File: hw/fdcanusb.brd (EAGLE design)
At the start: 41 x 32 mm, 42 parts, among them J1 MF-CON-MICROUSB-RIGHT, J3 JST-ZH6SMT_VERT, M1 MOUNT, M2 MOUNT, M3 MOUNT, M4 MOUNT, U1 MF-REG-SOT235-3.3V-300mA, U2 USBLC6-2SC6, U3 TCAN1057AEV, U4 TLP3317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

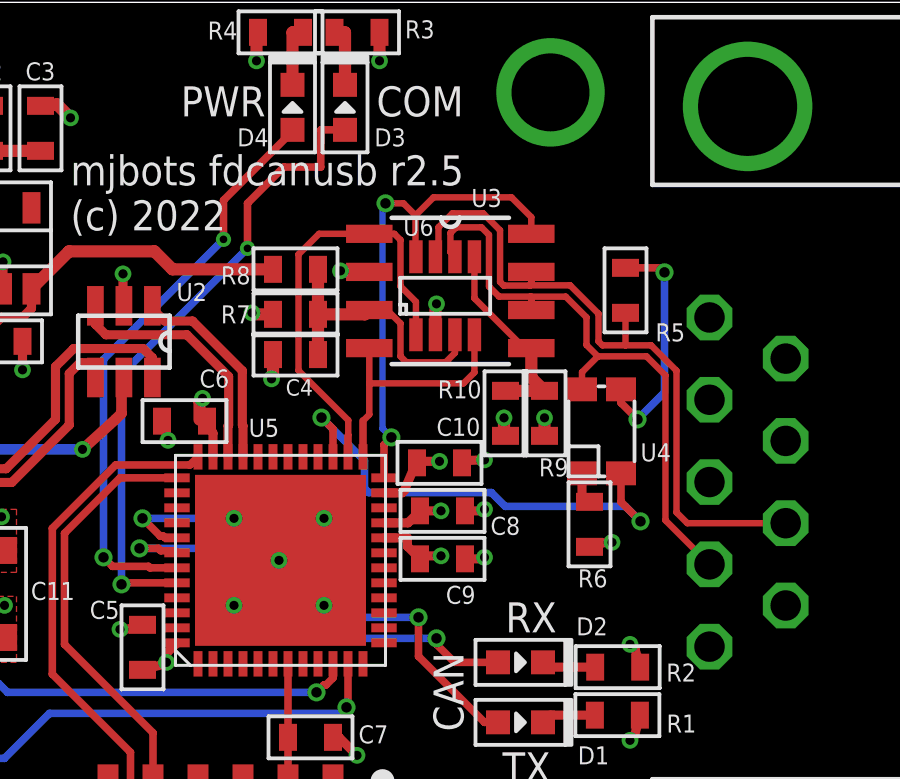
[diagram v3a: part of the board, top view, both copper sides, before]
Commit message: More silk tweaks
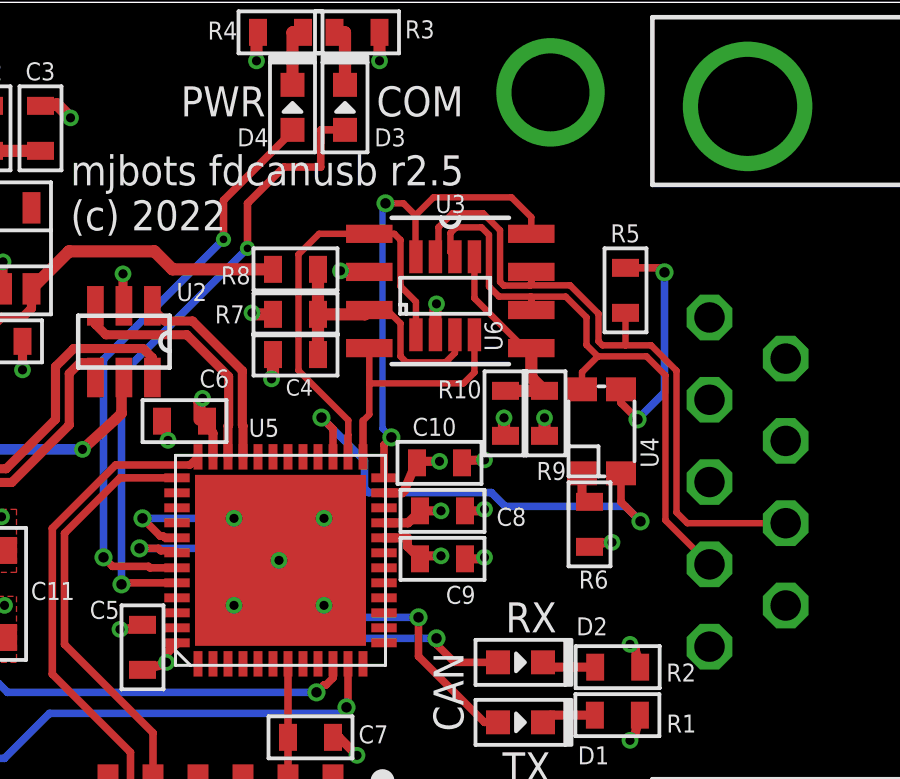
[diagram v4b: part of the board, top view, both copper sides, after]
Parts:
- R5: value 120 -> 110
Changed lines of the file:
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@@
 <attribute name="MF" value="TI" x="22.66" y="22.38" size="1.778" layer="27" display="off"/>
 <attribute name="MPN" value="TCAN1057AEVDRQ1" x="22.66" y="22.38" size="1.778" layer="27" display="off"/>
-<attribute name="NAME" x="23.36" y="25.18" size="0.6" layer="25" font="vector" ratio="10"/>
+<attribute name="NAME" x="22.16" y="24.98" size="0.6" layer="25" font="vector" ratio="10"/>
 <attribute name="POPULATE" value="1" x="22.66" y="22.38" size="1.778" layer="27" display="off"/>
 </element>
@@
 <attribute name="HOUSEPART" value="YES" x="64.21" y="-44.31" size="1.778" layer="27" display="off"/>
 <attribute name="MPN" value="MF-CAP-0603-0.1uF" x="64.21" y="-44.31" size="1.778" layer="27" display="off"/>
-<attribute name="NAME" x="22.2" y="17.55" size="0.6" layer="25" font="vector" ratio="10"/>
+<attribute name="NAME" x="21.4" y="17.55" size="0.6" layer="25" font="vector" ratio="10"/>
 <attribute name="POPULATE" value="1" x="64.21" y="-44.31" size="1.778" layer="27" display="off"/>
 <attribute name="TOLERANCE" value="" x="64.21" y="-44.31" size="1.778" layer="27" display="off"/>
@@
 <attribute name="HOUSEPART" value="YES" x="45.26" y="-45.91" size="1.778" layer="27" display="off"/>
 <attribute name="MPN" value="MF-CAP-0603-1uF" x="45.26" y="-45.91" size="1.778" layer="27" display="off"/>
-<attribute name="NAME" x="24" y="14.25" size="0.6" layer="25" font="vector" ratio="10"/>
+<attribute name="NAME" x="24.2" y="14.55" size="0.6" layer="25" font="vector" ratio="10"/>
 <attribute name="POPULATE" value="1" x="45.26" y="-45.91" size="1.778" layer="27" display="off"/>
 <attribute name="TOLERANCE" value="" x="45.26" y="-45.91" size="1.778" layer="27" display="off"/>
@@
 <attribute name="POPULATE" value="0" x="5" y="8" size="1.778" layer="27" display="off"/>
 </element>
-<element name="R5" library="mfpassives" package="R0603" value="120" x="28.5" y="22.4" smashed="yes" rot="R90">
+<element name="R5" library="mfpassives" package="R0603" value="110" x="28.5" y="22.4" smashed="yes" rot="R90">
 <attribute name="HOUSEPART" value="" x="28.5" y="22.4" size="1.778" layer="27" rot="R90" display="off"/>
 <attribute name="MF" value="YAGEO" x="28.5" y="22.4" size="1.778" layer="27" rot="R90" display="off"/>
-<attribute name="MPN" value="RC0603FR-07120RL" x="28.5" y="22.4" size="1.778" layer="27" rot="R90" display="off"/>
-<attribute name="NAME" x="29.5" y="20.7" size="0.6" layer="25" font="vector" ratio="10"/>
+<attribute name="MPN" value="RC0603FR-07110RL" x="28.5" y="22.4" size="1.778" layer="27" rot="R90" display="off"/>
+<attribute name="NAME" x="28" y="24" size="0.6" layer="25" font="vector" ratio="10"/>
 <attribute name="POPULATE" value="1" x="28.5" y="22.4" size="1.778" layer="27" rot="R90" display="off"/>
 <attribute name="TOLERANCE" value="" x="28.5" y="22.4" size="1.778" layer="27" rot="R90" display="off"/>
@@
 <attribute name="MF" value="TOSHIBA" x="27.7" y="17.7" size="1.778" layer="27" display="off"/>
 <attribute name="MPN" value="TLP3317" x="27.7" y="17.7" size="1.778" layer="27" display="off"/>
-<attribute name="NAME" x="29" y="16.7" size="0.6" layer="25" font="vector" ratio="10"/>
+<attribute name="NAME" x="29" y="17.5" size="0.6" layer="25" font="vector" ratio="10" rot="R270"/>
 <attribute name="POPULATE" value="1" x="27.7" y="17.7" size="1.778" layer="27" display="off"/>
 </element>
@@
 <attribute name="HOUSEPART" value="YES" x="27.3" y="14.6" size="1.778" layer="27" rot="R90" display="off"/>
 <attribute name="MPN" value="MF-RES-0603-330" x="27.3" y="14.6" size="1.778" layer="27" rot="R90" display="off"/>
-<attribute name="NAME" x="27.9" y="13.1" size="0.6" layer="25" font="vector" ratio="10" rot="R180"/>
+<attribute name="NAME" x="27.93" y="13.06" size="0.6" layer="25" font="vector" ratio="10" rot="R180"/>
 <attribute name="POPULATE" value="1" x="27.3" y="14.6" size="1.778" layer="27" rot="R90" display="off"/>
 <attribute name="TOLERANCE" value="" x="27.3" y="14.6" size="1.778" layer="27" rot="R90" display="off"/>
@@
 <attribute name="HOUSEPART" value="YES" x="17.5" y="21.6" size="1.778" layer="27" display="off"/>
 <attribute name="MPN" value="" x="17.5" y="21.6" size="1.778" layer="27" display="off"/>
-<attribute name="NAME" x="16" y="21.9" size="0.6" layer="25" font="vector" ratio="10" rot="R180"/>
+<attribute name="NAME" x="15.8" y="21.9" size="0.6" layer="25" font="vector" ratio="10" rot="R180"/>
 <attribute name="POPULATE" value="0" x="17.5" y="21.6" size="1.778" layer="27" display="off"/>
 <attribute name="TOLERANCE" value="" x="17.5" y="21.6" size="1.778" layer="27" display="off"/>
@@
 <attribute name="MF" value="TI" x="18.89" y="27.02" size="1.778" layer="27" display="off"/>
 <attribute name="MPN" value="TCAN334GDCNT" x="18.89" y="27.02" size="1.778" layer="27" display="off"/>
-<attribute name="NAME" x="21.09" y="24.22" size="0.6" layer="25" font="vector" ratio="10"/>
+<attribute name="NAME" x="24.4" y="20.38" size="0.6" layer="25" font="vector" ratio="10" rot="R90"/>
 <attribute name="POPULATE" value="0" x="18.89" y="27.02" size="1.778" layer="27" display="off"/>
 </element>
@@
 <attribute name="HOUSEPART" value="YES" x="25.8" y="18.3" size="1.778" layer="27" rot="R90" display="off"/>
 <attribute name="MPN" value="" x="25.8" y="18.3" size="1.778" layer="27" rot="R90" display="off"/>
-<attribute name="NAME" x="26.6" y="16.8" size="0.6" layer="25" font="vector" ratio="10" rot="R180"/>
+<attribute name="NAME" x="26.52" y="16.68" size="0.6" layer="25" font="vector" ratio="10" rot="R180"/>
 <attribute name="POPULATE" value="0" x="25.8" y="18.3" size="1.778" layer="27" rot="R90" display="off"/>
 <attribute name="TOLERANCE" value="" x="25.8" y="18.3" size="1.778" layer="27" rot="R90" display="off"/>

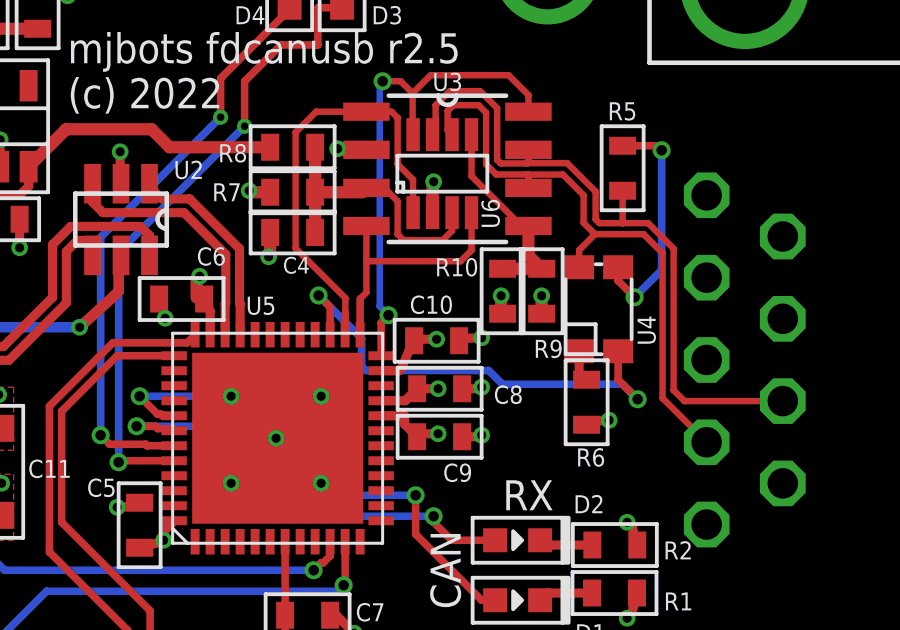
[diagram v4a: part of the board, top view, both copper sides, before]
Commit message: Add a decoupling cap on VIO
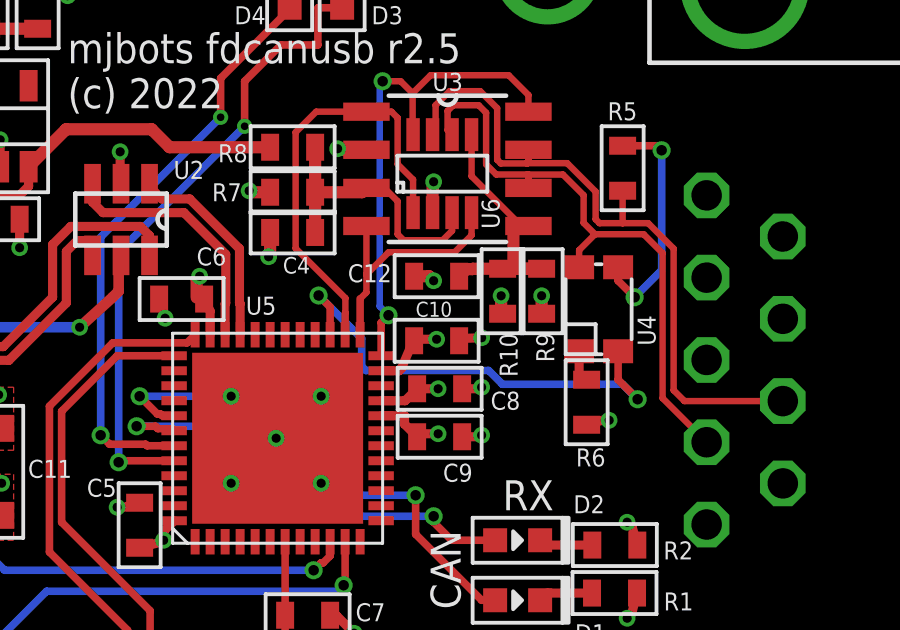
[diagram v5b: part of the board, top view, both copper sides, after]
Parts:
- added C12: 0.1uF, mfpassives:C0603
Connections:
- net CAN_SHDN_VIO: now also C12.P$1
- net GND: now also C12.P$2
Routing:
- net CAN_SHDN_VIO: track 6.87 -> 9.69 mm
- net GND: track 29.3 -> 30.0 mm, vias 33 -> 34
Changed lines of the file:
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@@
 <attribute name="HOUSEPART" value="YES" x="64.21" y="-44.31" size="1.778" layer="27" display="off"/>
 <attribute name="MPN" value="MF-CAP-0603-0.1uF" x="64.21" y="-44.31" size="1.778" layer="27" display="off"/>
-<attribute name="NAME" x="21.4" y="17.55" size="0.6" layer="25" font="vector" ratio="10"/>
+<attribute name="NAME" x="21.6" y="17.45" size="0.5" layer="25" font="vector" ratio="10"/>
 <attribute name="POPULATE" value="1" x="64.21" y="-44.31" size="1.778" layer="27" display="off"/>
 <attribute name="TOLERANCE" value="" x="64.21" y="-44.31" size="1.778" layer="27" display="off"/>
@@
 <attribute name="HOUSEPART" value="YES" x="45.26" y="-45.91" size="1.778" layer="27" display="off"/>
 <attribute name="MPN" value="MF-CAP-0603-1uF" x="45.26" y="-45.91" size="1.778" layer="27" display="off"/>
-<attribute name="NAME" x="24.2" y="14.55" size="0.6" layer="25" font="vector" ratio="10"/>
+<attribute name="NAME" x="24.1" y="14.35" size="0.6" layer="25" font="vector" ratio="10"/>
 <attribute name="POPULATE" value="1" x="45.26" y="-45.91" size="1.778" layer="27" display="off"/>
 <attribute name="TOLERANCE" value="" x="45.26" y="-45.91" size="1.778" layer="27" display="off"/>
@@
 <attribute name="HOUSEPART" value="YES" x="25.8" y="18.3" size="1.778" layer="27" rot="R90" display="off"/>
 <attribute name="MPN" value="" x="25.8" y="18.3" size="1.778" layer="27" rot="R90" display="off"/>
-<attribute name="NAME" x="26.52" y="16.68" size="0.6" layer="25" font="vector" ratio="10" rot="R180"/>
+<attribute name="NAME" x="25.62" y="16.92" size="0.6" layer="25" font="vector" ratio="10" rot="R270"/>
 <attribute name="POPULATE" value="0" x="25.8" y="18.3" size="1.778" layer="27" rot="R90" display="off"/>
 <attribute name="TOLERANCE" value="" x="25.8" y="18.3" size="1.778" layer="27" rot="R90" display="off"/>
@@
 <attribute name="HOUSEPART" value="YES" x="24.5" y="18.3" size="1.778" layer="27" rot="R270" display="off"/>
 <attribute name="MPN" value="MF-RES-0603-0" x="24.5" y="18.3" size="1.778" layer="27" rot="R270" display="off"/>
-<attribute name="NAME" x="23.7" y="19.4" size="0.6" layer="25" font="vector" ratio="10" rot="R180"/>
+<attribute name="NAME" x="24.4" y="16.9" size="0.6" layer="25" font="vector" ratio="10" rot="R270"/>
 <attribute name="POPULATE" value="1" x="24.5" y="18.3" size="1.778" layer="27" rot="R270" display="off"/>
 <attribute name="TOLERANCE" value="" x="24.5" y="18.3" size="1.778" layer="27" rot="R270" display="off"/>
@@
 <attribute name="VOLTAGE" value="" x="24.5" y="18.3" size="1.778" layer="27" rot="R270" display="off"/>
 <attribute name="WATTAGE" value="" x="24.5" y="18.3" size="1.778" layer="27" rot="R270" display="off"/>
+</element>
+<element name="C12" library="mfpassives" package="C0603" value="0.1uF" x="22.3" y="18.8" smashed="yes" rot="R180">
+<attribute name="DIELECTRIC" value="" x="22.3" y="18.8" size="1.778" layer="27" rot="R180" display="off"/>
+<attribute name="HOUSEPART" value="YES" x="22.3" y="18.8" size="1.778" layer="27" rot="R180" display="off"/>
+<attribute name="MPN" value="MF-CAP-0603-0.1uF" x="22.3" y="18.8" size="1.778" layer="27" rot="R180" display="off"/>
+<attribute name="NAME" x="20.8" y="19.2" size="0.6" layer="25" font="vector" ratio="10" rot="R180"/>
+<attribute name="POPULATE" value="1" x="22.3" y="18.8" size="1.778" layer="27" rot="R180" display="off"/>
+<attribute name="TOLERANCE" value="" x="22.3" y="18.8" size="1.778" layer="27" rot="R180" display="off"/>
+<attribute name="URL" value="" x="22.3" y="18.8" size="1.778" layer="27" rot="R180" display="off"/>
+<attribute name="VOLTAGE" value="" x="22.3" y="18.8" size="1.778" layer="27" rot="R180" display="off"/>
 </element>
 </elements>
@@
 <wire x1="16.75" y1="20.26" x2="16.75" y2="19.5" width="0.4064" layer="1"/>
 <wire x1="16.75" y1="19.5" x2="16.7" y2="19.45" width="0.4064" layer="1"/>
+<contactref element="C12" pad="P$2"/>
+<via x="22.2" y="18.65" extent="1-16" drill="0.3048"/>
+<wire x1="21.55" y1="18.8" x2="22.05" y2="18.8" width="0.4064" layer="1"/>
+<wire x1="22.05" y1="18.8" x2="22.2" y2="18.65" width="0.4064" layer="1"/>
 </signal>
 <signal name="VBUS">
@@
 <contactref element="U6" pad="4"/>
 <wire x1="19.75" y1="18.05" x2="19.96" y2="18.26" width="0.2159" layer="1"/>
-<wire x1="19.96" y1="18.26" x2="19.96" y2="19.3" width="0.2159" layer="1"/>
-<wire x1="19.96" y1="19.3" x2="19.96" y2="20.475" width="0.2159" layer="1"/>
-<wire x1="23.465" y1="20.92" x2="23.465" y2="19.665" width="0.2159" layer="1"/>
-<wire x1="23.1" y1="19.3" x2="19.96" y2="19.3" width="0.2159" layer="1"/>
-<wire x1="23.465" y1="19.665" x2="23.1" y2="19.3" width="0.2159" layer="1"/>
+<wire x1="19.96" y1="18.26" x2="19.96" y2="18.86" width="0.2159" layer="1"/>
+<wire x1="19.96" y1="18.86" x2="19.96" y2="20.475" width="0.2159" layer="1"/>
+<wire x1="23.465" y1="20.92" x2="23.465" y2="20.165" width="0.2159" layer="1"/>
+<wire x1="22.9" y1="19.6" x2="20.7" y2="19.6" width="0.2159" layer="1"/>
+<wire x1="20.7" y1="19.6" x2="19.96" y2="18.86" width="0.2159" layer="1"/>
+<wire x1="23.465" y1="20.165" x2="22.9" y2="19.6" width="0.2159" layer="1"/>
 </signal>
 <signal name="CAN_TX">
@@
 <contactref element="R10" pad="P$1"/>
 <wire x1="24.5" y1="19.05" x2="25.8" y2="19.05" width="0.4064" layer="1"/>
-<wire x1="25.8" y1="19.05" x2="25.36" y2="19.49" width="0.4064" layer="1"/>
-<wire x1="25.36" y1="19.49" x2="25.36" y2="20.475" width="0.4064" layer="1"/>
+<wire x1="25.8" y1="19.05" x2="24.86" y2="19.05" width="0.4064" layer="1"/>
+<wire x1="24.86" y1="20.475" x2="24.86" y2="19.05" width="0.4064" layer="1"/>
+<wire x1="24.86" y1="20.475" x2="25.36" y2="20.475" width="0.4064" layer="1"/>
+<contactref element="C12" pad="P$1"/>
+<wire x1="23.05" y1="18.8" x2="23.28645" y2="19.03645" width="0.4064" layer="1"/>
+<wire x1="23.28645" y1="19.03645" x2="23.4920125" y2="19.03645" width="0.4064" layer="1"/>
+<wire x1="23.4920125" y1="19.03645" x2="23.5055625" y2="19.05" width="0.4064" layer="1"/>
+<wire x1="23.5055625" y1="19.05" x2="24.5" y2="19.05" width="0.4064" layer="1"/>
 </signal>
 </signals>
